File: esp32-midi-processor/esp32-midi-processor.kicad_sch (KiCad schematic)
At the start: 22 parts, among them J1 AudioJack3, J2 AudioJack3, J3 AudioJack3, J4 AudioJack3, J5 Conn_01x15_Socket, J6 Conn_01x15_Socket, U1 6N138, U2 6N138

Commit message: add more stuff to schematic
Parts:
- added J7: Input Voltage, symbol Connector:Conn_01x02_Socket
- J1: value AudioJack3 -> Midi IN 1
- J2: value AudioJack3 -> Midi IN 2
- J3: value AudioJack3 -> Midi OUT 1
- J4: value AudioJack3 -> Midi OUT 2
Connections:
- net +3V3: now also J5.15 (Pin_15)
- net +5V: now also C1.1, C2.1
- net GND: now also C1.2, C2.2, J5.14 (Pin_14), J6.14 (Pin_14), J7.1 (Pin_1)
- net RX0: now reaches R2.2, U1.6 (VO2)
- net RX0: now also J5.4 (Pin_4)
- net D16: now reaches R5.2, U2.6 (VO2)
- net D16: now also J5.10 (Pin_10)
- net D23: now reaches J5.1 (Pin_1)
- net D4: now reaches J5.11 (Pin_11)
- net D2: now reaches J5.12 (Pin_12)
- net D15: now reaches J5.13 (Pin_13)
- net D22: now reaches J5.2 (Pin_2)
- net TX0: now reaches J5.3 (Pin_3)
- net TX0: now also R8.2
- net D21: now reaches J5.5 (Pin_5)
- net D19: now reaches J5.6 (Pin_6)
- net D18: now reaches J5.7 (Pin_7)
- net D5: now reaches J5.8 (Pin_8)
- net D17: now reaches J5.9 (Pin_9)
- net D17: now also R10.2
- net EN: now reaches J6.1 (Pin_1)
- net D27: now reaches J6.10 (Pin_10)
- net D14: now reaches J6.11 (Pin_11)
- net D12: now reaches J6.12 (Pin_12)
- net D13: now reaches J6.13 (Pin_13)
- net VIN: now reaches J6.15 (Pin_15)
- net VIN: now also J7.2 (Pin_2)
- net VP: now reaches J6.2 (Pin_2)
- net VN: now reaches J6.3 (Pin_3)
- net D34: now reaches J6.4 (Pin_4)
- net D35: now reaches J6.5 (Pin_5)
- net D32: now reaches J6.6 (Pin_6)
- net D33: now reaches J6.7 (Pin_7)
- net D25: now reaches J6.8 (Pin_8)
- net D26: now reaches J6.9 (Pin_9)
- no-connect marks 0 -> 3
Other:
- moved on the sheet: C1, C2, J5, J6

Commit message: add more stuff to schematic
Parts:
- added C3, C4, C5, C6, C7: 0.1µ, Capacitor_SMD:C_0603_1608Metric, symbol Device:C
- added D3, D4, D5, D6, D7: WS2812B, LED_SMD:LED_WS2812B_PLCC4_5.0x5.0mm_P3.2mm, symbol LED:WS2812B
- added J10: USB Shield right, symbol Connector:Conn_01x12_Socket
- added J11: Rotary Encoder, symbol Connector:Conn_01x05_Socket
- added J12: Display, symbol Connector:Conn_01x04_Socket
- added J8: USB Shield outer left, symbol Connector:Conn_01x12_Socket
- added J9: USB Shield inner left, symbol Connector:Conn_01x05_Socket
- added JP1: Cut trace on Shield when bridged, symbol Jumper:SolderJumper_2_Open
- added R11: 330, symbol Device:R
- J5: value Conn_01x15_Socket -> ESP32 right
- J6: value Conn_01x15_Socket -> ESP32 left
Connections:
- net +3V3: now also J11.1 (Pin_1)
- net +5V: now also C3.1, C4.1, C5.1, C6.1, C7.1, D3.1 (VDD), D4.1 (VDD), D5.1 (VDD), D6.1 (VDD), D7.1 (VDD), J12.1 (Pin_1), JP1.2 (B)
- net D15: now also J8.10 (Pin_10)
- net D18: now also J10.4 (Pin_4)
- net D19: now also J10.3 (Pin_3)
- net D23: now also J10.2 (Pin_2)
- net D25: now also J11.2 (Pin_2)
- net D26: now also J11.3 (Pin_3)
- net D27: now also J11.4 (Pin_4)
- net D34: now also R11.2
- net D5: now also J10.1 (Pin_1)
- net GND: now also C3.2, C4.2, C5.2, C6.2, C7.2, D3.3 (VSS), D4.3 (VSS), D5.3 (VSS), D6.3 (VSS), D7.3 (VSS), J10.11 (Pin_11), J11.5 (Pin_5), J12.4 (Pin_4), J8.9 (Pin_9)
- new net: D5.2 (DOUT), D6.4 (DIN)
- new net: D4.2 (DOUT), D5.4 (DIN)
- new net: J9.1 (Pin_1), JP1.1 (A)
- new net: D3.2 (DOUT), D4.4 (DIN)
- new net: D6.2 (DOUT), D7.4 (DIN)
- new net LED_DATA: D3.4 (DIN), R11.1
- no-connect marks 3 -> 24
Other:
- moved on the sheet: J5

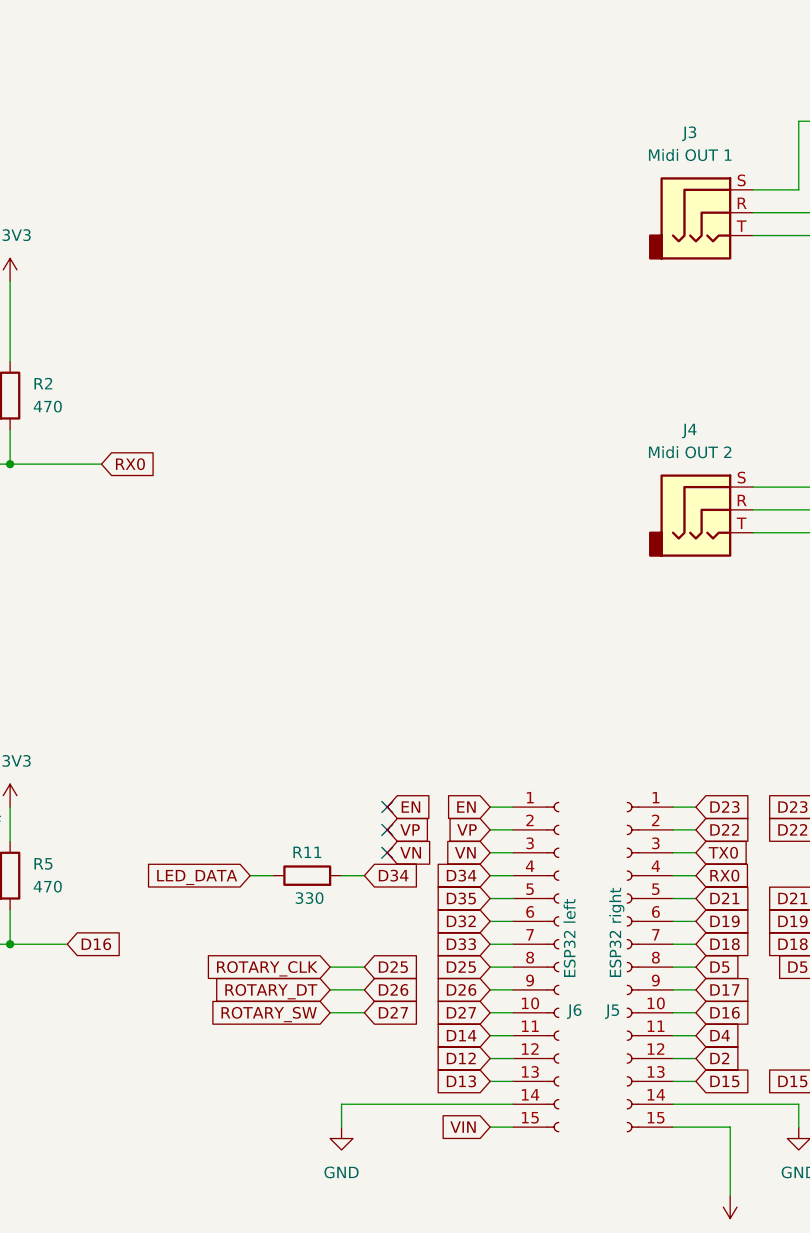
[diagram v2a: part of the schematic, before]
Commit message: add switches, disconnect rotary encoder
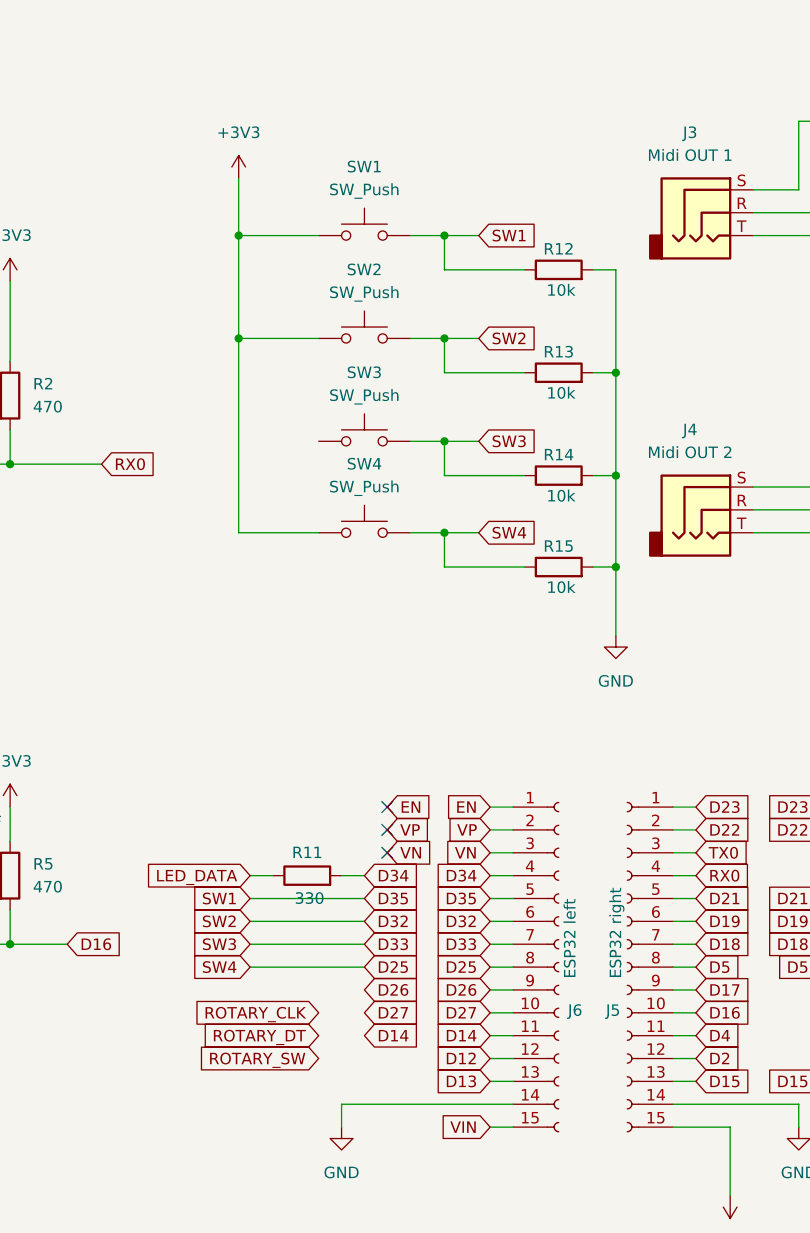
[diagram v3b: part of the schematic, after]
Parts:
- added R12, R13, R14, R15: 10k, symbol Device:R
- added SW1, SW2, SW3, SW4: SW_Push, symbol Switch:SW_Push
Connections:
- net +3V3: now also SW1.1, SW2.1, SW4.1
- net D25: now also R15.1, SW4.2; no longer J11.2 (Pin_2)
- net D26: no longer J11.3 (Pin_3)
- net D27: no longer J11.4 (Pin_4)
- net D32: now also R13.1, SW2.2
- net D33: now also R14.1, SW3.2
- net D35: now also R12.1, SW1.2
- net GND: now also R12.2, R13.2, R14.2, R15.2
- new net ROTARY_CLK: J11.2 (Pin_2)
- new net ROTARY_DT: J11.3 (Pin_3)
- new net ROTARY_SW: J11.4 (Pin_4)

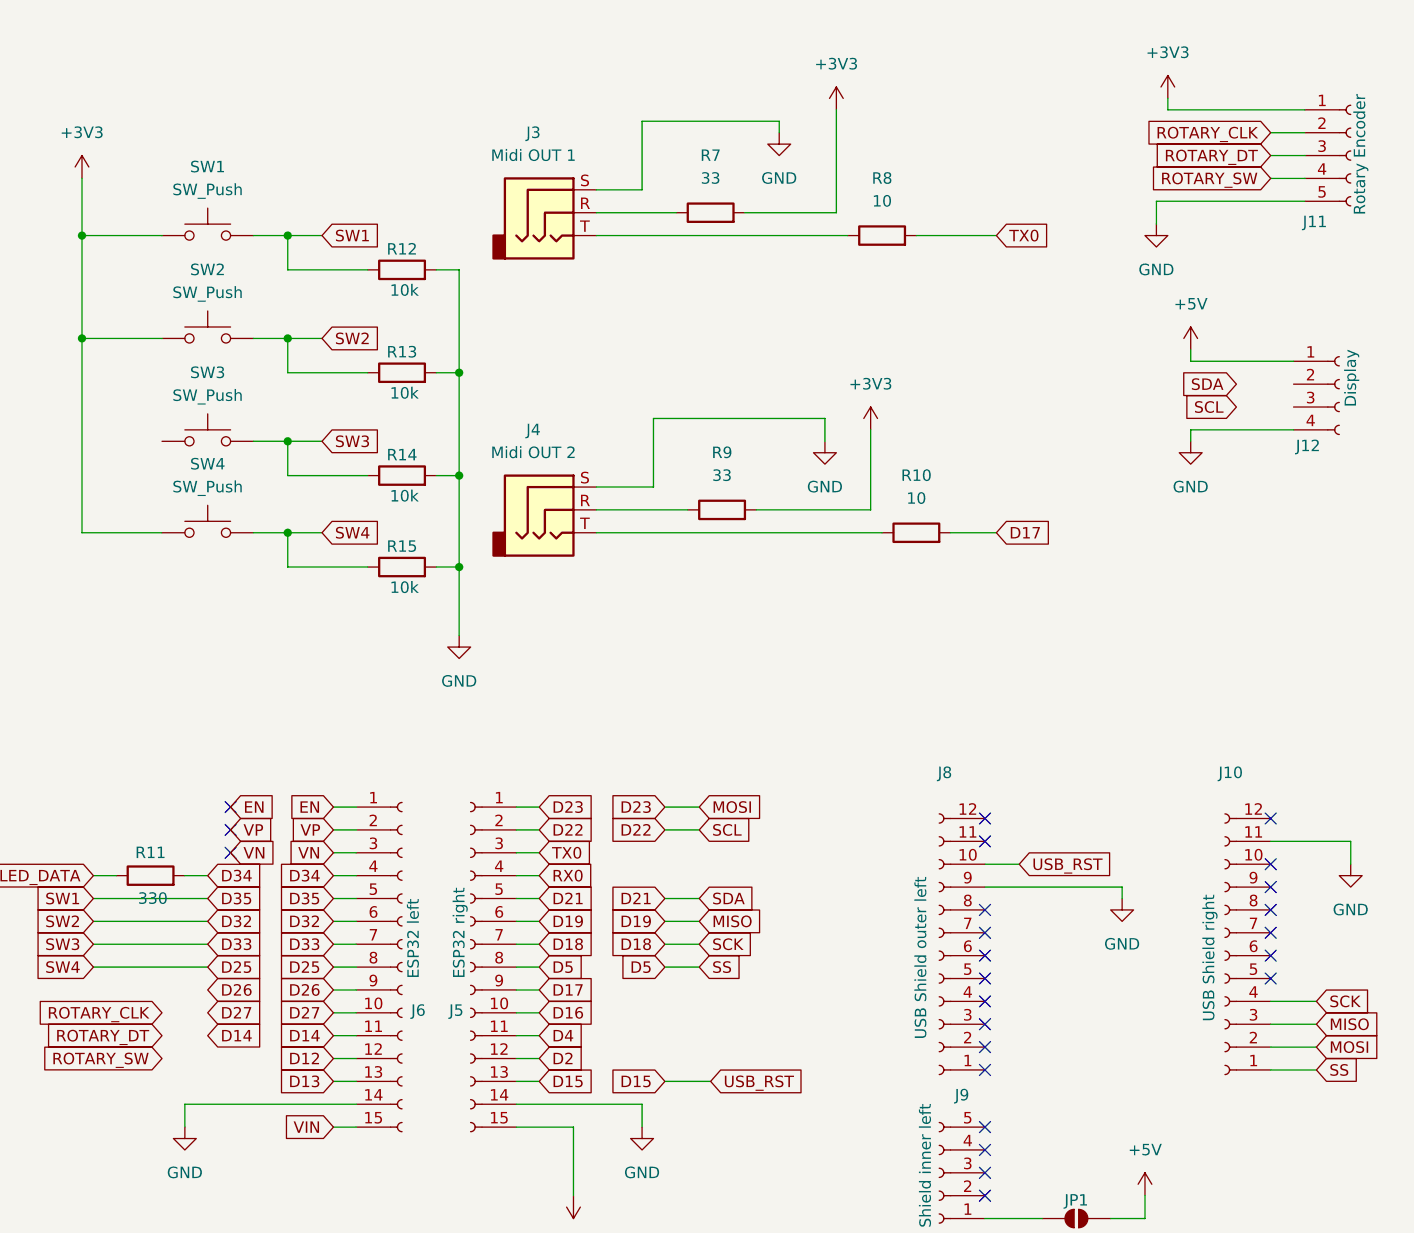
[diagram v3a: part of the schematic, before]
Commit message: fix rotary encoder
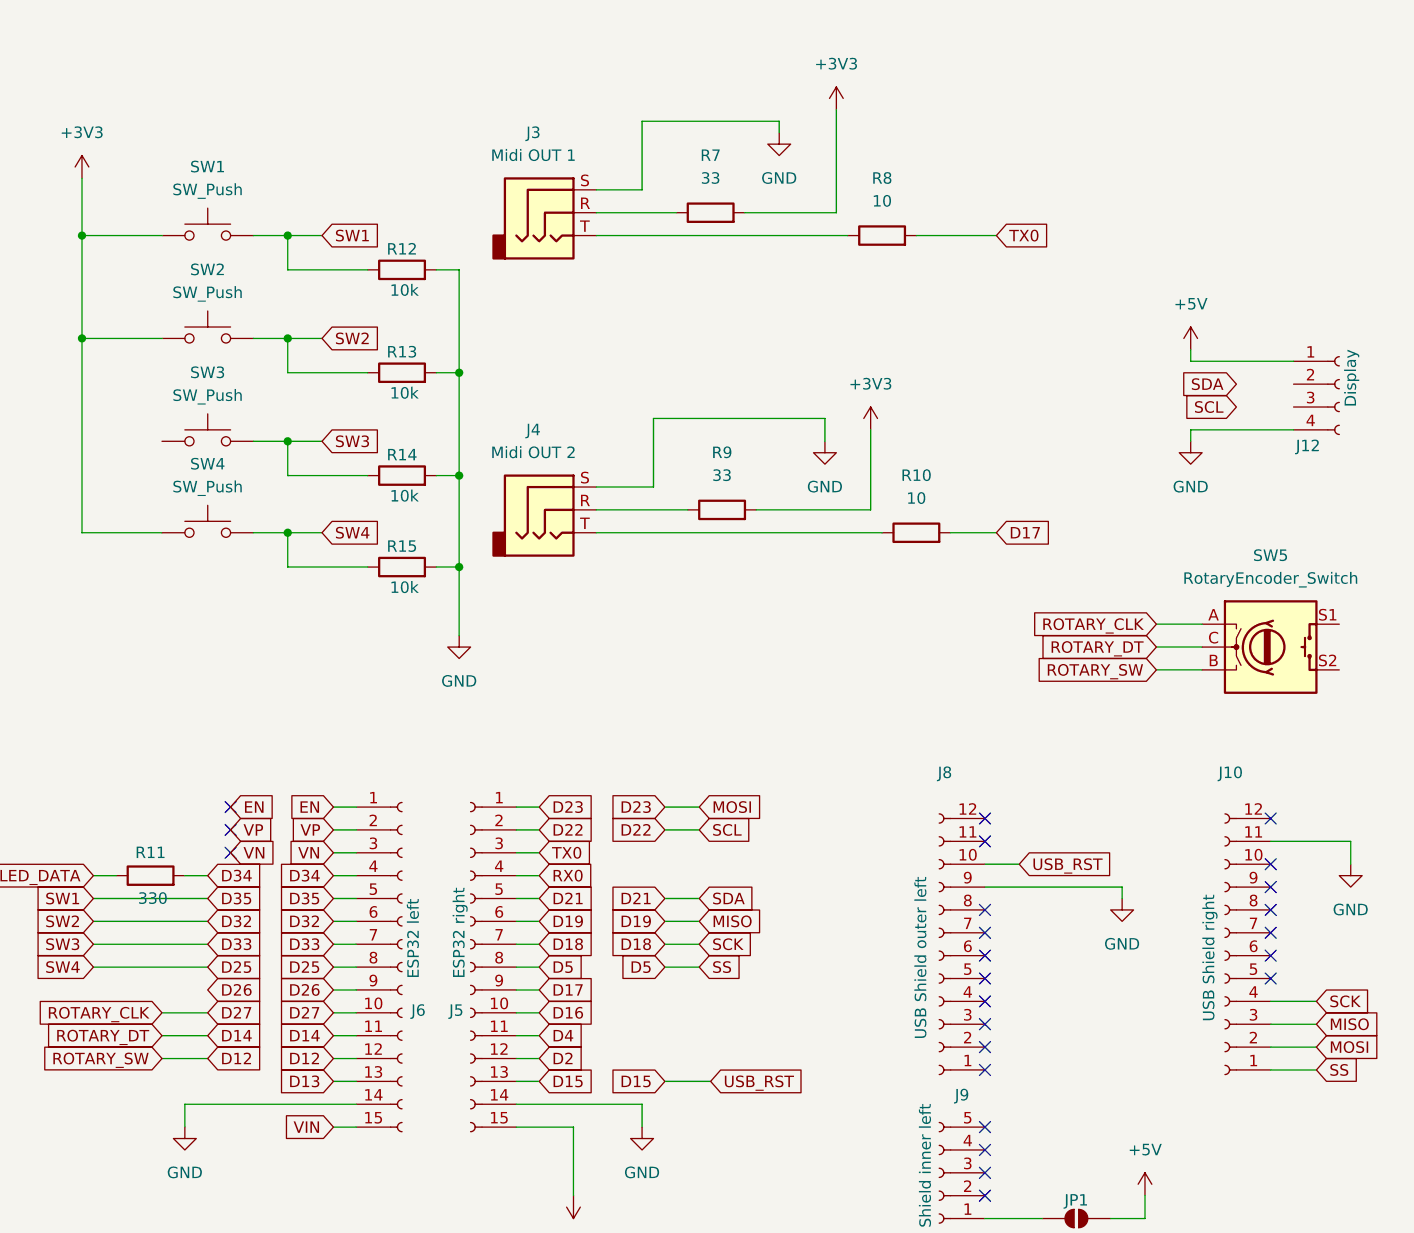
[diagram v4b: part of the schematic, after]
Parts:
- removed J11: Rotary Encoder, symbol Connector:Conn_01x05_Socket
- added SW5: RotaryEncoder_Switch, symbol Device:RotaryEncoder_Switch
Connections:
- net D12: now also SW5.B
- net D14: now also SW5.C
- net D27: now also SW5.A

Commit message: add footprints
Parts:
- added J11: Spare, Connector_PinHeader_2.54mm:PinHeader_1x05_P2.54mm_Vertical, symbol Connector:Conn_01x05_Socket
- added R16: 10k, Resistor_SMD:R_0603_1608Metric, symbol Device:R
- J1, J2, J3, J4: footprint (none) -> Connector_Audio:Jack_3.5mm_CUI_SJ-3523-SMT_Horizontal
- J10, J8: footprint (none) -> Connector_PinHeader_2.54mm:PinHeader_1x12_P2.54mm_Vertical
- J5, J6: footprint (none) -> Connector_PinHeader_2.54mm:PinHeader_1x15_P2.54mm_Vertical
- J7: footprint (none) -> TerminalBlock_RND:TerminalBlock_RND_205-00001_1x02_P5.00mm_Horizontal
- J9: footprint (none) -> Connector_PinHeader_2.54mm:PinHeader_1x05_P2.54mm_Vertical
- R1, R10, R11, R12, R13, R14, R15, R2, R3, R4, R5, R6, R7, R8, R9: footprint (none) -> Resistor_SMD:R_0603_1608Metric
- SW1, SW2, SW3, SW4: footprint (none) -> Button_Switch_THT:SW_PUSH-12mm_Wuerth-430476085716
- SW5: footprint (none) -> Rotary_Encoder:RotaryEncoder_Alps_EC11E-Switch_Vertical_H20mm
- U1: footprint (none) -> Package_DIP:DIP-8_W7.62mm_Socket
- U2: footprint (none) -> dip-8_w7.62mm_Socket
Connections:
- net +3V3: now also SW3.1, SW5.S1, J11.2 (Pin_2)
- net +5V: now also J12.2 (Pin_2); no longer J12.1 (Pin_1)
- net D12: now also SW5.C; no longer SW5.B
- net D13: now also J11.3 (Pin_3)
- net D14: now also SW5.B; no longer SW5.C
- net D2: now also J11.5 (Pin_5)
- net D21: now also J12.4 (Pin_4)
- net D22: now also J12.3 (Pin_3)
- net D26: now also SW5.S2, R16.2
- net D4: now also J11.4 (Pin_4)
- net GND: now also J12.1 (Pin_1), J11.1 (Pin_1), R16.1; no longer J12.4 (Pin_4)
- no-connect marks 24 -> 27
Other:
- moved on the sheet: J7, SW5

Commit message: first pcb version
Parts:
- C1, C2: footprint (none) -> Capacitor_SMD:C_0603_1608Metric
- J12: footprint (none) -> Connector_PinHeader_2.54mm:PinHeader_1x04_P2.54mm_Vertical
- JP1: footprint (none) -> Jumper:SolderJumper-2_P1.3mm_Open_RoundedPad1.0x1.5mm
- U2: footprint dip-8_w7.62mm_Socket -> Package_DIP:DIP-8_W7.62mm_Socket
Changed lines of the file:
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@@
 			)
 		)
-		(property "Footprint" "dip-8_w7.62mm_Socket"
+		(property "Footprint" "Package_DIP:DIP-8_W7.62mm_Socket"
 			(at 84.836 121.92 0)
 			(effects
@@
 			)
 		)
-		(property "Footprint" ""
+		(property "Footprint" "Connector_PinHeader_2.54mm:PinHeader_1x04_P2.54mm_Vertical"
 			(at 276.86 54.61 0)
 			(effects
@@
 			)
 		)
-		(property "Footprint" ""
+		(property "Footprint" "Jumper:SolderJumper-2_P1.3mm_Open_RoundedPad1.0x1.5mm"
 			(at 247.65 147.32 0)
 			(effects
@@
 			)
 		)
-		(property "Footprint" ""
+		(property "Footprint" "Capacitor_SMD:C_0603_1608Metric"
 			(at 101.2952 48.26 0)
 			(effects
@@
 			)
 		)
-		(property "Footprint" ""
+		(property "Footprint" "Capacitor_SMD:C_0603_1608Metric"
 			(at 102.5652 106.68 0)
 			(effects

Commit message: Next PCB version
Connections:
- net +5V: now also D3.3 (VDD), D4.3 (VDD), D5.3 (VDD), D6.3 (VDD), D7.3 (VDD); no longer D3.1 (VDD), D4.1 (VDD), D5.1 (VDD), D6.1 (VDD), D7.1 (VDD)
- net GND: now also D3.1 (VSS), D4.1 (VSS), D5.1 (VSS), D6.1 (VSS), D7.1 (VSS); no longer D3.3 (VSS), D4.3 (VSS), D5.3 (VSS), D6.3 (VSS), D7.3 (VSS)
- net LED_DATA: now also D3.2 (DIN); no longer D3.4 (DIN)
- net at D5.2 (DIN): now also D4.4 (DOUT); no longer D6.4 (DIN)
- net at D5.4 (DOUT): now also D6.2 (DIN); no longer D4.2 (DOUT)
- net at D7.4 (DOUT): no longer D6.2 (DOUT)
- net at D7.2 (DIN): now also D6.4 (DOUT)
- new net: D3.4 (DOUT), D4.2 (DIN)
